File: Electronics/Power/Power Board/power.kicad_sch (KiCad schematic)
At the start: 119 parts, among them IC202 TLV1805DBVR, IC205 MP28167GQ-A-Z, IC206 TPS563202DRLR, IC207 TPS563202DRLR, IC208 TLV1805DBVR, IC3 INA219AIDR, J2 Screw_Terminal_01x02, J201 Pluggable_Terminal_01x02, J201 XT60PW-F, J202 JST-XH-2.50mm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

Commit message: Sensor hub board done
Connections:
- no-connect marks 1 -> 5
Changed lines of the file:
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@@
   (junction (at 204.47 151.13) (diameter 0) (color 0 0 0 0)
   )
+  (no_connect (at 46.99 46.99))
   (no_connect (at 83.82 44.45))
+  (no_connect (at 379.73 36.83))
+  (no_connect (at 379.73 44.45))
+  (no_connect (at 46.99 39.37))
   (wire (pts (xy 35.56 133.35) (xy 35.56 130.81))
     (stroke (width 0) (type default))
@@
     (pin "1")
     (pin "2")
+    (pin "SH1")
+    (pin "SH2")
     (instances
       (project "Power Board"
@@
     (pin "1")
     (pin "2")
+    (pin "SH1")
+    (pin "SH2")
     (instances
       (project "Power Board"

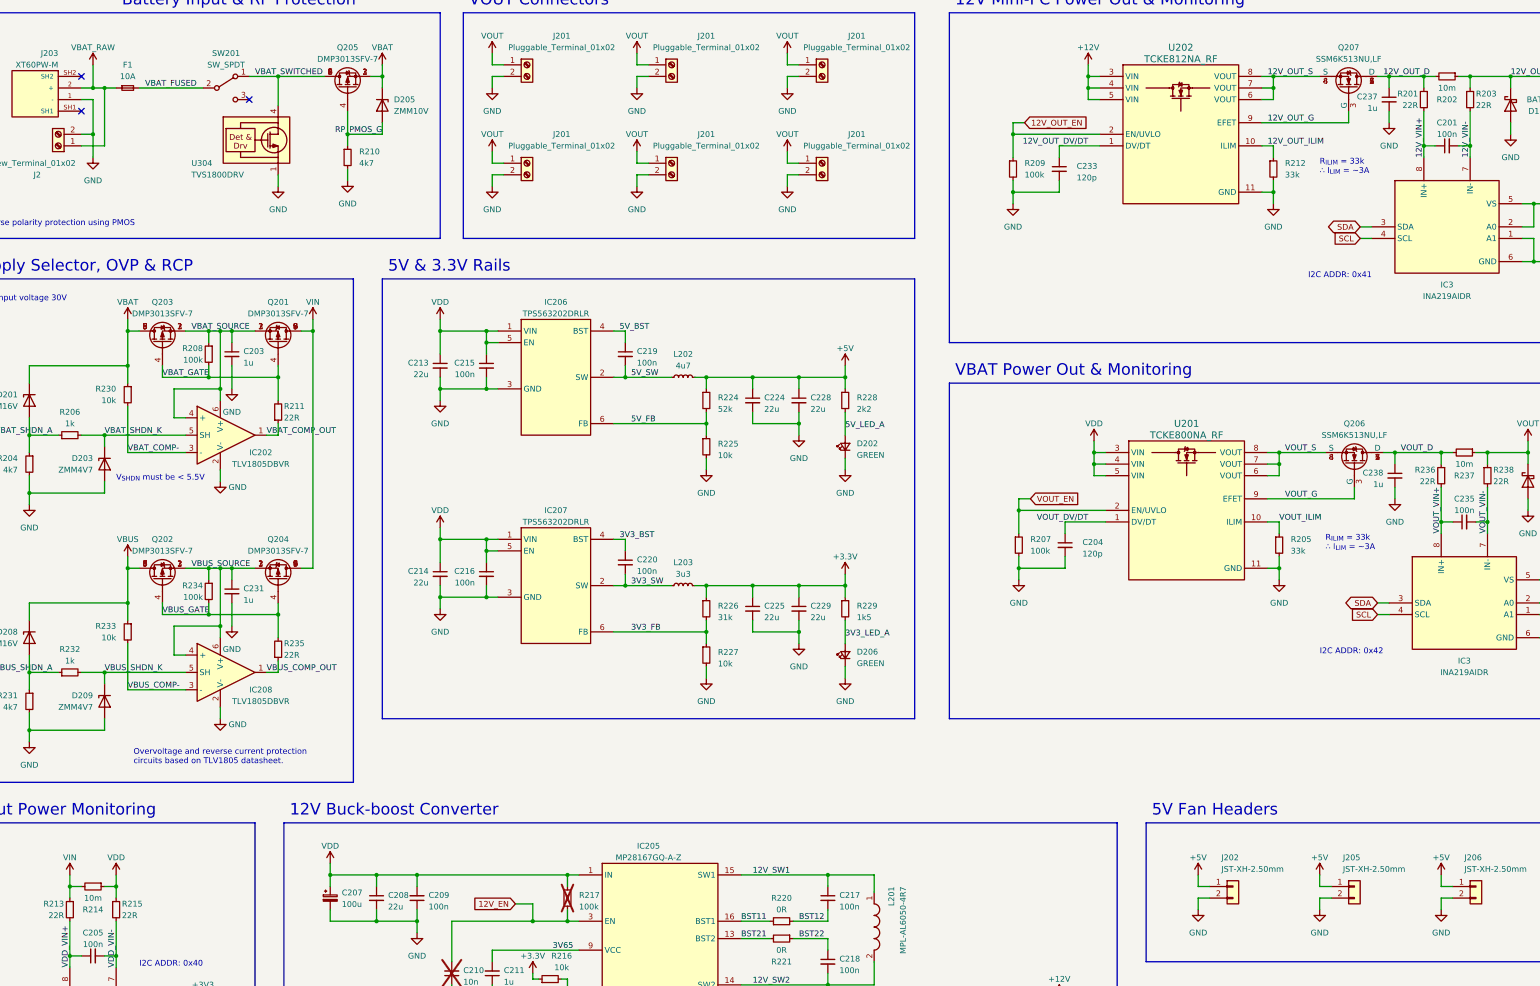
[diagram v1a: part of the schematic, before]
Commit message: Motor driver and power boards done
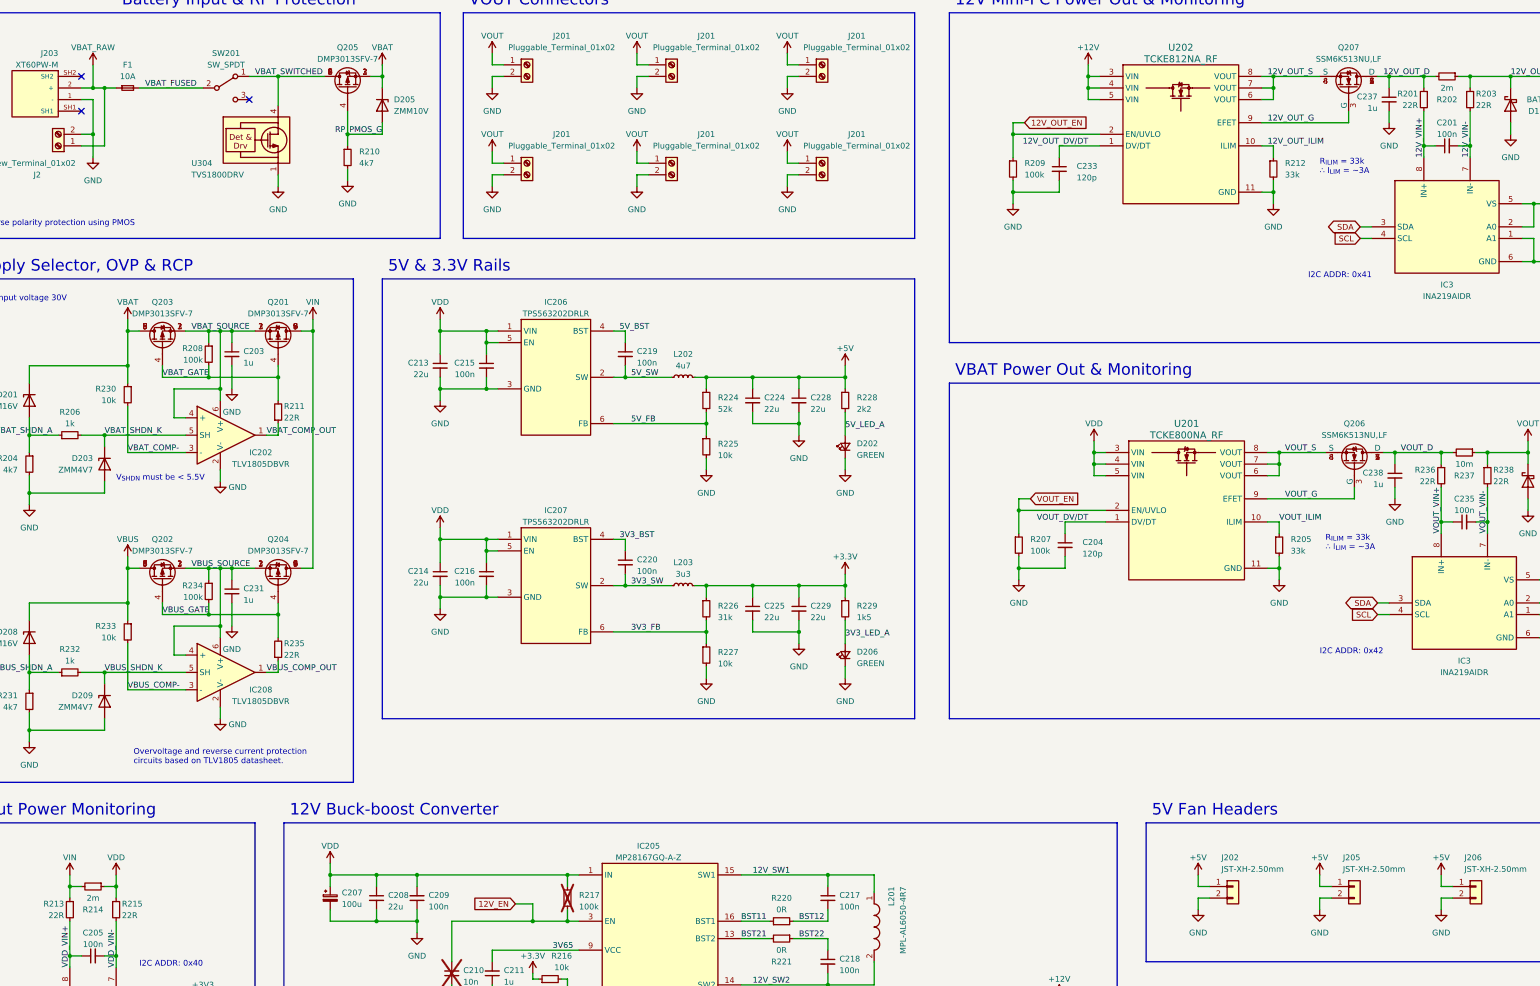
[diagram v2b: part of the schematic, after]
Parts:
- R202, R214: value 10m -> 2m
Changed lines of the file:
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@@
       (effects (font (size 1.27 1.27)))
     )
-    (property "Value" "10m" (at 49.53 219.71 90)
+    (property "Value" "2m" (at 49.53 219.71 90)
       (effects (font (size 1.27 1.27)))
     )
@@
       (effects (font (size 1.27 1.27)))
     )
-    (property "Value" "10m" (at 346.71 41.91 90)
-      (effects (font (size 1.27 1.27)))
-    )
+    (property "Value" "2m" (at 346.71 41.91 90)
+      (effects (font (size 1.27 1.27)))
+    )

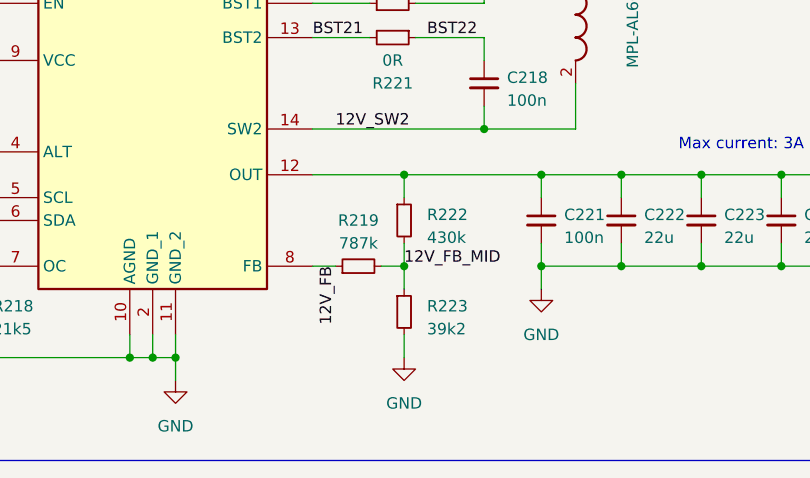
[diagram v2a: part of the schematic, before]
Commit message: Added "ibom"s for PCBs
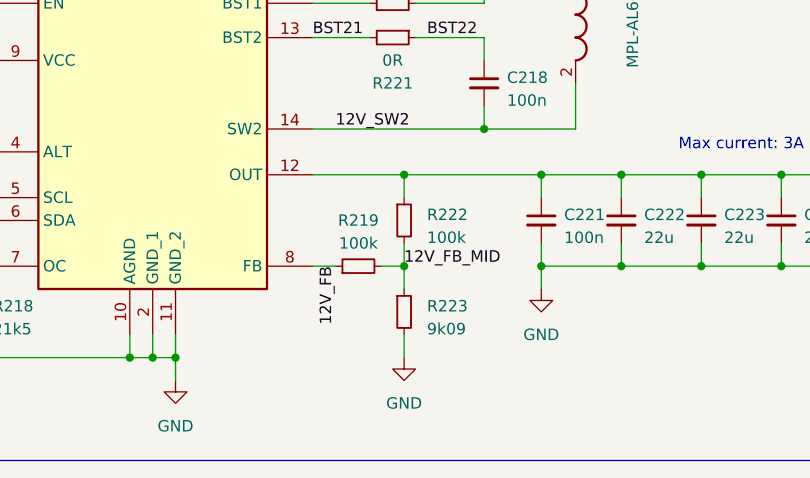
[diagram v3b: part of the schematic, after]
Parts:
- R219: value 787k -> 100k
- R222: value 430k -> 100k
- R223: value 39k2 -> 9k09
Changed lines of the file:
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@@
       (effects (font (size 1.27 1.27)) (justify left))
     )
-    (property "Value" "39k2 " (at 204.47 260.985 0)
+    (property "Value" "9k09" (at 204.47 260.985 0)
       (effects (font (size 1.27 1.27)) (justify left))
     )
@@
       (effects (font (size 1.27 1.27)))
     )
-    (property "Value" "787k" (at 196.85 251.46 90)
+    (property "Value" "100k" (at 196.85 251.46 90)
       (effects (font (size 1.27 1.27)))
     )
@@
       (effects (font (size 1.27 1.27)) (justify left))
     )
-    (property "Value" "430k" (at 204.47 250.825 0)
-      (effects (font (size 1.27 1.27)) (justify left))
-    )
+    (property "Value" "100k" (at 204.47 250.825 0)
+      (effects (font (size 1.27 1.27)) (justify left))
+    )
